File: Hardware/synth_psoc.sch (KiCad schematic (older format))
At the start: 0 parts

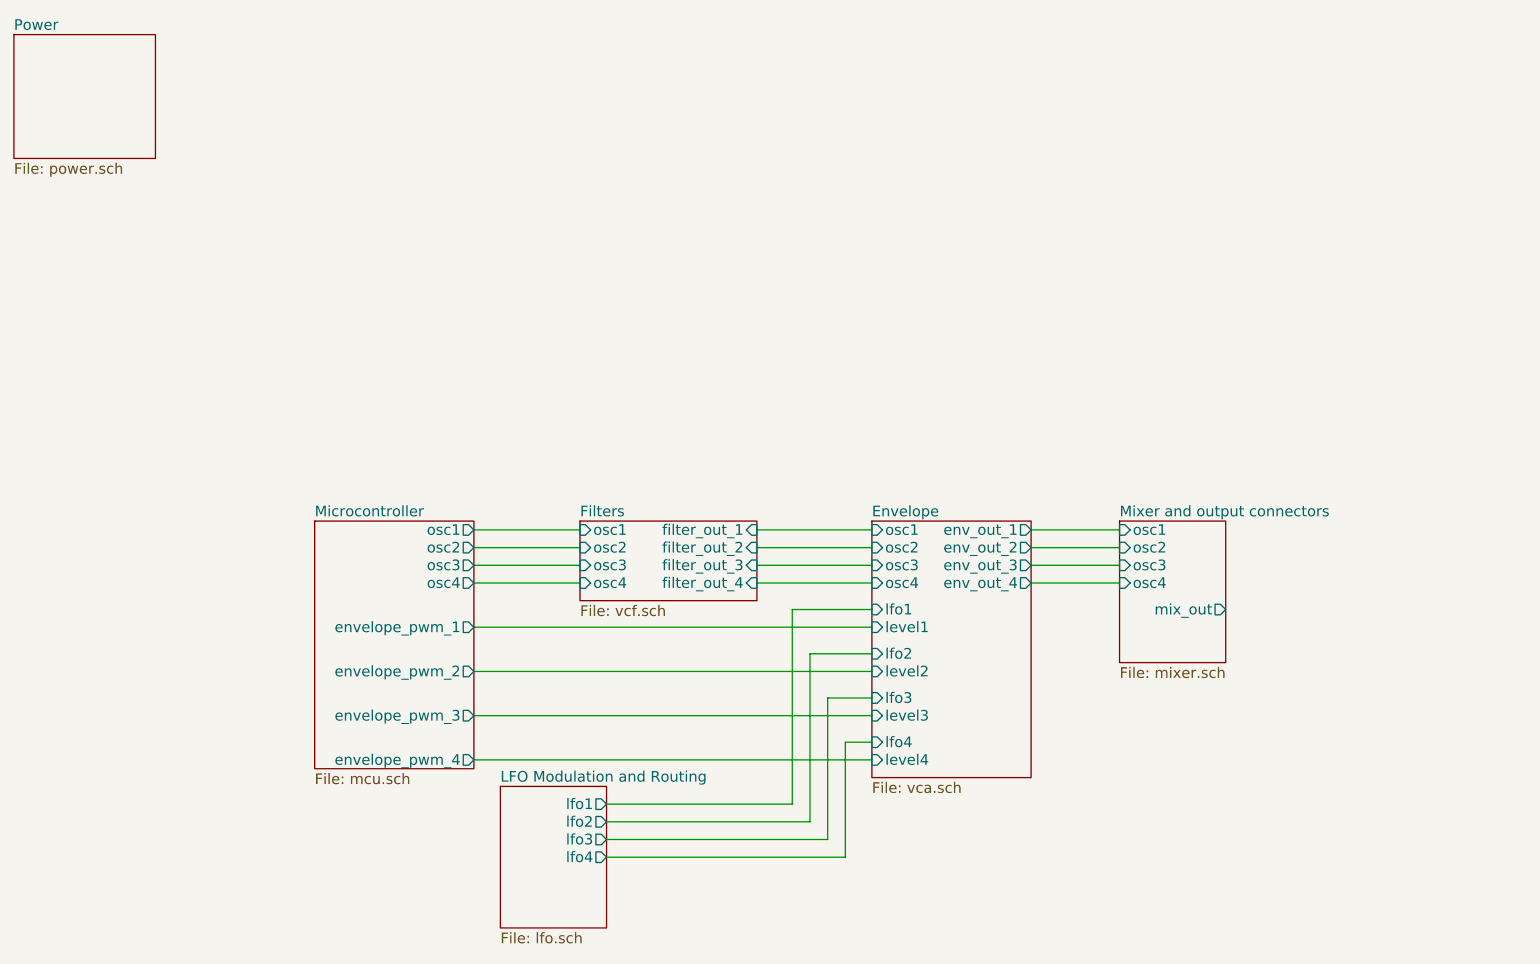
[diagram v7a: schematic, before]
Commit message: change corner frequency of DC blocking caps  everywhere they are in use.  Updated some simulation files to test filter circuits.
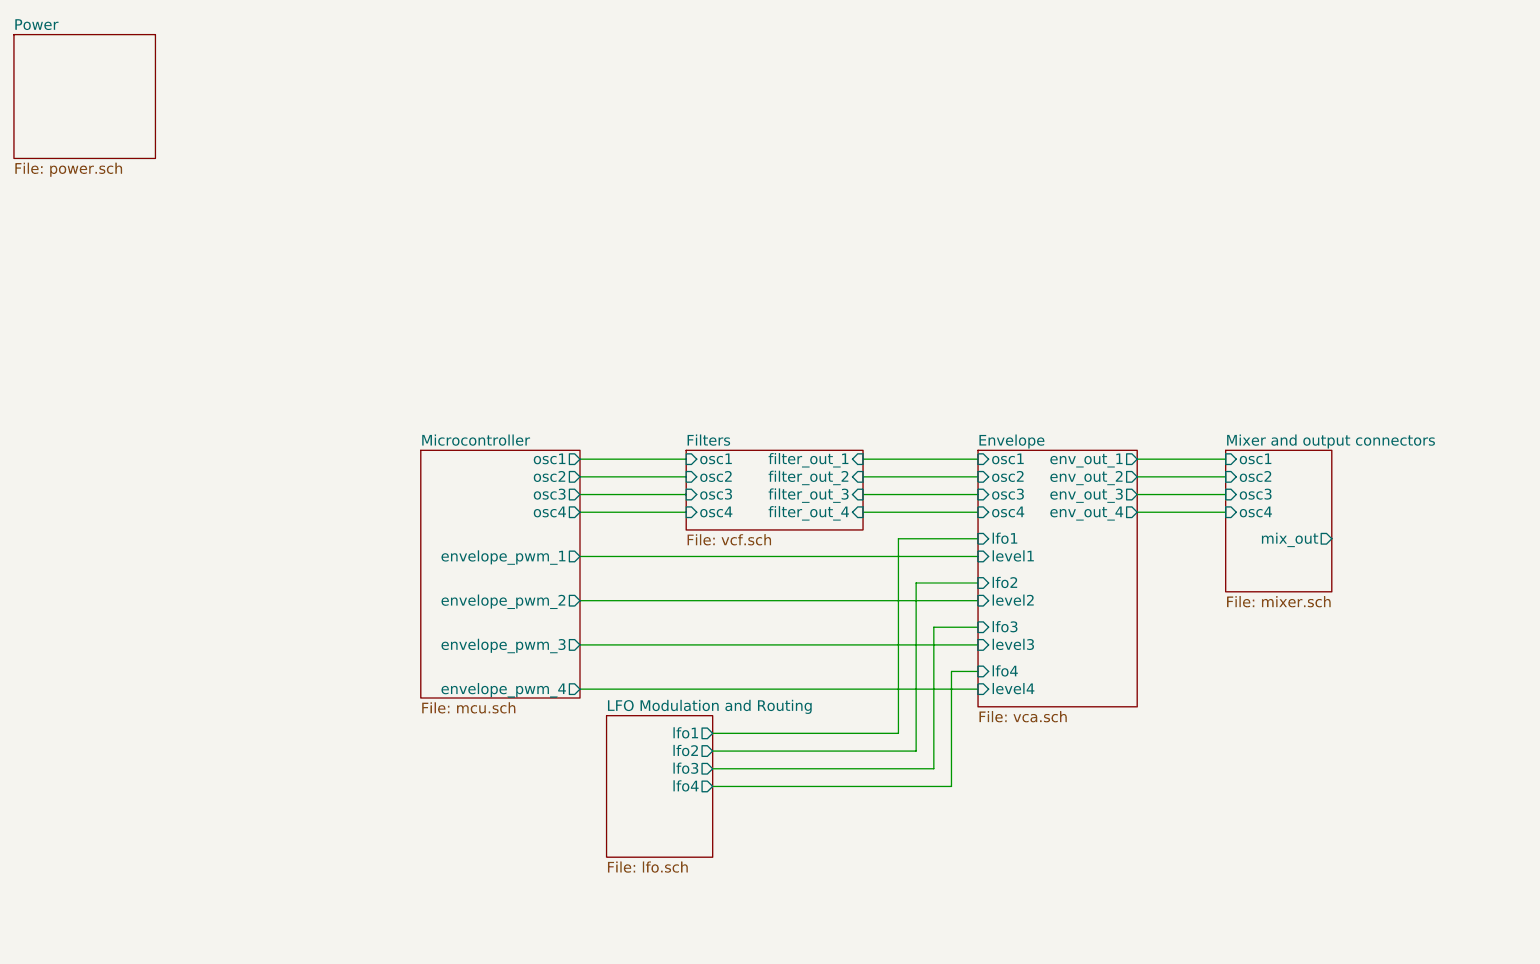
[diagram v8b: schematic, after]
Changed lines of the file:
@@
 $EndDescr
 $Sheet
-S 3850 3400 1000 450
+S 4450 3000 1000 450
 U 5C355489
 F0 "Filters" 60
 F1 "vcf.sch" 60
-F2 "osc1" I L 3850 3450 60
-F3 "osc2" I L 3850 3550 60
-F4 "osc3" I L 3850 3650 60
-F5 "osc4" I L 3850 3750 60
-F6 "filter_out_1" I R 4850 3450 60
-F7 "filter_out_2" I R 4850 3550 60
-F8 "filter_out_3" I R 4850 3650 60
-F9 "filter_out_4" I R 4850 3750 60
+F2 "osc1" I L 4450 3050 60
+F3 "osc2" I L 4450 3150 60
+F4 "osc3" I L 4450 3250 60
+F5 "osc4" I L 4450 3350 60
+F6 "filter_out_1" I R 5450 3050 60
+F7 "filter_out_2" I R 5450 3150 60
+F8 "filter_out_3" I R 5450 3250 60
+F9 "filter_out_4" I R 5450 3350 60
 $EndSheet
 $Sheet
@@
 $EndSheet
 $Sheet
-S 5500 3400 900  1450
+S 6100 3000 900  1450
 U 5C356D9E
 F0 "Envelope" 60
 F1 "vca.sch" 60
-F2 "osc1" I L 5500 3450 60
-F3 "osc2" I L 5500 3550 60
-F4 "osc3" I L 5500 3650 60
-F5 "osc4" I L 5500 3750 60
-F6 "lfo1" I L 5500 3900 60
-F7 "level1" I L 5500 4000 60
-F8 "env_out_1" O R 6400 3450 60
-F9 "lfo2" I L 5500 4150 60
-F10 "level2" I L 5500 4250 60
-F11 "env_out_2" O R 6400 3550 60
-F12 "lfo3" I L 5500 4400 60
-F13 "level3" I L 5500 4500 60
-F14 "env_out_3" O R 6400 3650 60
-F15 "lfo4" I L 5500 4650 60
-F16 "level4" I L 5500 4750 60
-F17 "env_out_4" O R 6400 3750 60
+F2 "osc1" I L 6100 3050 60
+F3 "osc2" I L 6100 3150 60
+F4 "osc3" I L 6100 3250 60
+F5 "osc4" I L 6100 3350 60
+F6 "lfo1" I L 6100 3500 60
+F7 "level1" I L 6100 3600 60
+F8 "env_out_1" O R 7000 3050 60
+F9 "lfo2" I L 6100 3750 60
+F10 "level2" I L 6100 3850 60
+F11 "env_out_2" O R 7000 3150 60
+F12 "lfo3" I L 6100 4000 60
+F13 "level3" I L 6100 4100 60
+F14 "env_out_3" O R 7000 3250 60
+F15 "lfo4" I L 6100 4250 60
+F16 "level4" I L 6100 4350 60
+F17 "env_out_4" O R 7000 3350 60
 $EndSheet
 $Sheet
-S 6900 3400 600  800
+S 7500 3000 600  800
 U 5C357081
 F0 "Mixer and output connectors" 60
 F1 "mixer.sch" 60
-F2 "osc1" I L 6900 3450 60
-F3 "osc2" I L 6900 3550 60
-F4 "osc3" I L 6900 3650 60
-F5 "osc4" I L 6900 3750 60
-F6 "mix_out" O R 7500 3900 60
+F2 "osc1" I L 7500 3050 60
+F3 "osc2" I L 7500 3150 60
+F4 "osc3" I L 7500 3250 60
+F5 "osc4" I L 7500 3350 60
+F6 "mix_out" O R 8100 3500 60
 $EndSheet
 $Sheet
-S 3400 4900 600  800
+S 4000 4500 600  800
 U 5C35738C
 F0 "LFO Modulation and Routing" 60
 F1 "lfo.sch" 60
-F2 "lfo1" O R 4000 5000 60
-F3 "lfo2" O R 4000 5100 60
-F4 "lfo3" O R 4000 5200 60
-F5 "lfo4" O R 4000 5300 60
+F2 "lfo1" O R 4600 4600 60
+F3 "lfo2" O R 4600 4700 60
+F4 "lfo3" O R 4600 4800 60
+F5 "lfo4" O R 4600 4900 60
 $EndSheet
 Wire Wire Line
-	3250 3450 3850 3450
+	3850 3050 4450 3050
 Wire Wire Line
-	3250 3550 3850 3550
+	3850 3150 4450 3150
 Wire Wire Line
-	3250 3650 3850 3650
+	3850 3250 4450 3250
 Wire Wire Line
-	3250 3750 3850 3750
+	3850 3350 4450 3350
 Wire Wire Line
-	4850 3450 5500 3450
+	5450 3050 6100 3050
 Wire Wire Line
-	4850 3550 5500 3550
+	5450 3150 6100 3150
 Wire Wire Line
-	4850 3650 5500 3650
+	5450 3250 6100 3250
 Wire Wire Line
-	4850 3750 5500 3750
+	5450 3350 6100 3350
 Wire Wire Line
-	6400 3450 6900 3450
+	7000 3050 7500 3050
 Wire Wire Line
-	6400 3550 6900 3550
+	7000 3150 7500 3150
 Wire Wire Line
-	6400 3650 6900 3650
+	7000 3250 7500 3250
 Wire Wire Line
-	6400 3750 6900 3750
+	7000 3350 7500 3350
 Wire Wire Line
-	4000 5000 5050 5000
+	4600 4600 5650 4600
 Wire Wire Line
-	5050 5000 5050 3900
+	5650 4600 5650 3500
 Wire Wire Line
-	5050 3900 5500 3900
+	5650 3500 6100 3500
 Wire Wire Line
-	5500 4150 5150 4150
+	6100 3750 5750 3750
 Wire Wire Line
-	5150 4150 5150 5100
+	5750 3750 5750 4700
 Wire Wire Line
-	5150 5100 4000 5100
+	5750 4700 4600 4700
 Wire Wire Line
-	5500 4400 5250 4400
+	6100 4000 5850 4000
 Wire Wire Line
-	5250 4400 5250 5200
+	5850 4000 5850 4800
 Wire Wire Line
-	5250 5200 4000 5200
+	5850 4800 4600 4800
 Wire Wire Line
-	5500 4650 5350 4650
+	6100 4250 5950 4250
 Wire Wire Line
-	5350 4650 5350 5300
+	5950 4250 5950 4900
 Wire Wire Line
-	5350 5300 4000 5300
+	5950 4900 4600 4900
 $Sheet
-S 2350 3400 900  1400
+S 2950 3000 900  1400
 U 5C3546FC
 F0 "Microcontroller" 60
 F1 "mcu.sch" 60
-F2 "osc1" O R 3250 3450 60
-F3 "osc2" O R 3250 3550 60
-F4 "osc3" O R 3250 3650 60
-F5 "osc4" O R 3250 3750 60
-F6 "envelope_pwm_1" O R 3250 4000 60
-F7 "envelope_pwm_2" O R 3250 4250 60
-F8 "envelope_pwm_3" O R 3250 4500 60
-F9 "envelope_pwm_4" O R 3250 4750 60
+F2 "osc1" O R 3850 3050 60
+F3 "osc2" O R 3850 3150 60
+F4 "osc3" O R 3850 3250 60
+F5 "osc4" O R 3850 3350 60
+F6 "envelope_pwm_1" O R 3850 3600 60
+F7 "envelope_pwm_2" O R 3850 3850 60
+F8 "envelope_pwm_3" O R 3850 4100 60
+F9 "envelope_pwm_4" O R 3850 4350 60
 $EndSheet
 Wire Wire Line
-	3250 4000 5500 4000
+	3850 3600 6100 3600
 Wire Wire Line
-	5500 4250 3250 4250
+	6100 3850 3850 3850
 Wire Wire Line
-	3250 4500 5500 4500
+	3850 4100 6100 4100
 Wire Wire Line
-	5500 4750 3250 4750
+	6100 4350 3850 4350
 $EndSCHEMATC
